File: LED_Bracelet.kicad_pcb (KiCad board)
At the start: 4 copper layers, 37.2 x 32.5 mm, 43 parts, among them J1 USB-C (Female), J2 LED Strip, J3 LED Filament, Q1 Si2301CDS, SW1 BOOT, U1 TP4056, U2 DW01A-G, U3 FS8205A, U4 TPS61170, U5 SN74AHCT1G125DBVR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

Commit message: Tweaks to the PCB
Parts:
- added H1: MountingHole_Pad, Custom:JLCPCB ToolingHole, F.Cu at (94.5, 38.7)
- added H2: MountingHole_Pad, Custom:JLCPCB ToolingHole, F.Cu at (63.5, 68.2)
- moved R14 1.59 mm to (98.5, 43.9), turned to 90 degrees
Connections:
- R14 pad 2: GND -> +BATT
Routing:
- net -BATT: track 21.2 -> 7.09 mm
- net +BATT: track 19.0 -> 21.3 mm, vias 4 -> 5
- net GND: track 31.2 -> 30.3 mm
- added copper zone on In2.Cu, net +5V
- added copper zone on In2.Cu, net -BATT
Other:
- board text added: "(analog)"
- board text added: "(digital)"
- board text added: "1A max"
- board text added: "1S LiPo USB-C ESP32-C3"
- board text added: "3v3"
- board text added: "5V"
- board text added: "BOOT"
- board text added: "ESP32-C3-WROOM-02"
- board text added: "LED Bracelet"
- board text added: "Power"
- board text added: "Standby Charging"
- board text added: "USB"
- board text added: "W"
- board text removed: "1S LiPo USB-C Multiple voltages"
- board text removed: "Rechargable Fan Controller"

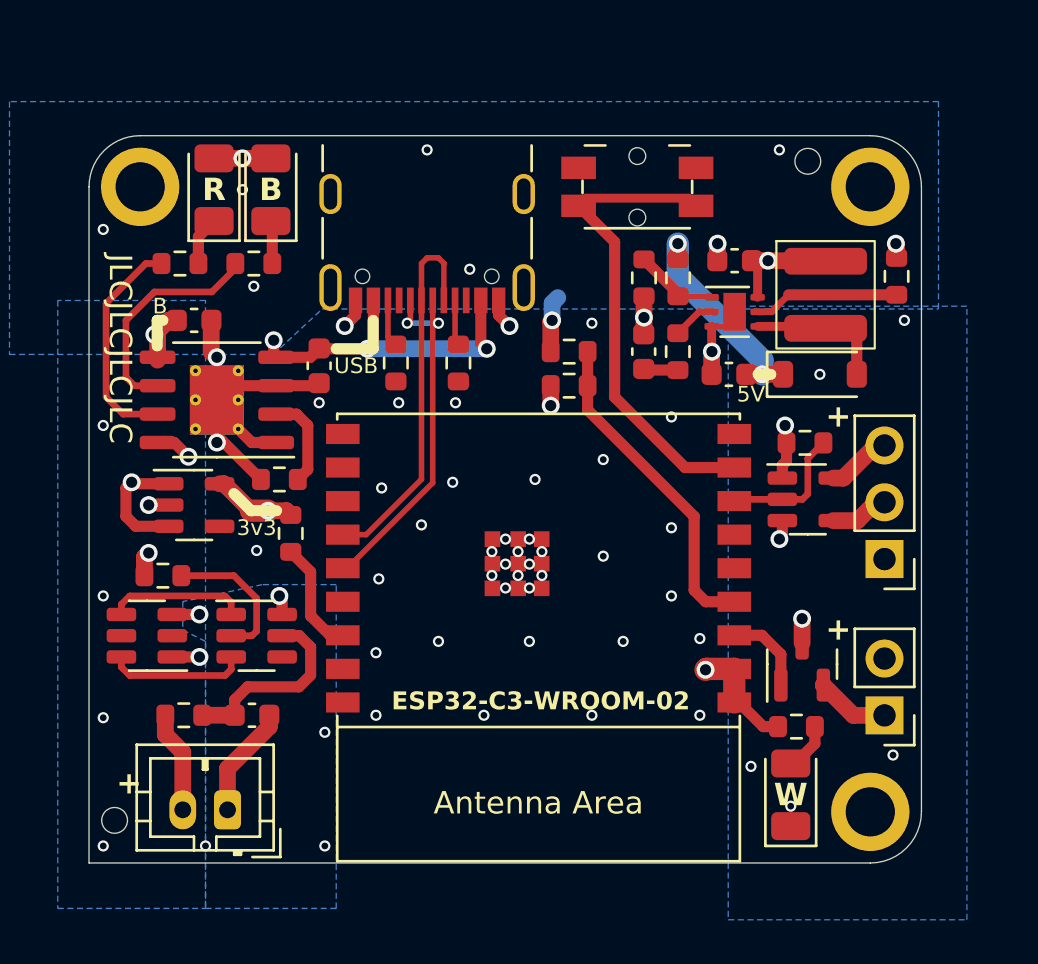
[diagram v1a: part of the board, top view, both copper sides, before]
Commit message: First software version + some PCB changes Separate BOOT and Mode buttons. LED Filament MOSFET (Q1) has pulldown resistor and is the correct channel. PlatformIO project + code. Frequently Asked Questions (FAQ).
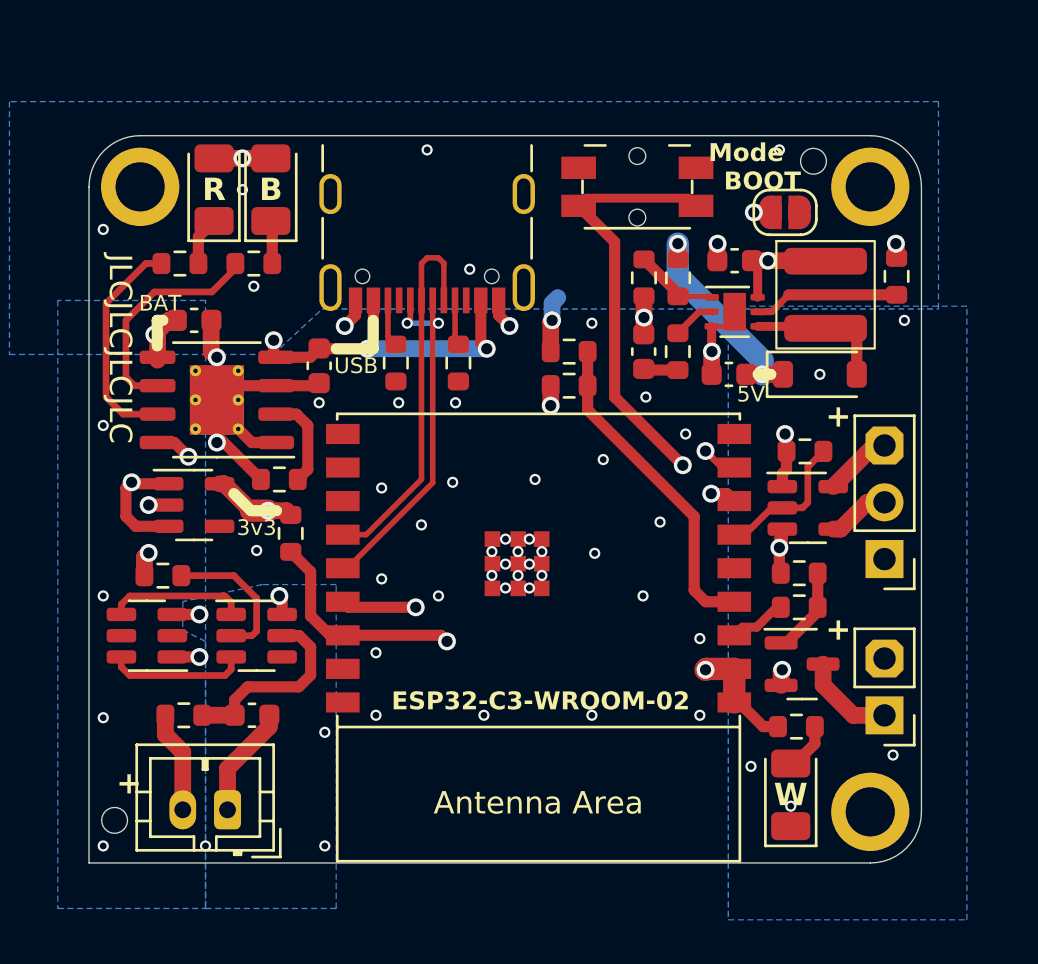
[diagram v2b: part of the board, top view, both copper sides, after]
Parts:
- added R17: 100R, Resistor_SMD:R_0603_1608Metric, F.Cu at (94.1, 58.7)
- added R18: 1k, Resistor_SMD:R_0603_1608Metric, F.Cu at (94.1, 57.1)
- added SW2: BOOT, Jumper:SolderJumper-2_P1.3mm_Open_RoundedPad1.0x1.5mm, F.Cu at (93.5, 41.0)
- Q1: value Si2301CDS -> AO3400A
- SW1: value BOOT -> Mode
- moved R11 0.38 mm to (94.4, 51.7)
- moved U5 0.38 mm to (94.5, 54.2)
- moved H1 0.25 mm to (94.7, 38.7)
- turned Q1 to 0 degrees
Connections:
- Q1 pad 1: LED Filament -> /Q1 Gate
- Q1 pad 2: Net-(J3-Pin_1) -> GND
- Q1 pad 3: GND -> Net-(J3-Pin_1)
- R12 pad 2: /Strapping 1 -> Strapping_1
- SW1 pad 2: /BOOT -> /Mode
- U6 pad 15: unconnected-(U6-GPIO3/ADC1_CH3-Pad15) -> /Mode
- U6 pad 16: /Strapping 1 -> Strapping_1
- U6 pad 6: unconnected-(U6-GPIO7-Pad6) -> LED Strip
- U6 pad 7: LED Strip -> Strapping_1
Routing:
- net /Mode: track 0.00 -> 40.8 mm, vias 0 -> 2
- net Strapping_1: track 0.00 -> 28.2 mm, vias 0 -> 2
- net /Strapping 1: track 5.03 -> 0.00 mm
- net /Q1 Gate: track 0.00 -> 3.93 mm
- net /BOOT: track 21.4 -> 19.3 mm, vias 0 -> 2
- net LED Filament: track 3.81 -> 2.60 mm
- net Net-(J3-Pin_1): track 3.30 -> 4.24 mm
- net GND: track 30.3 -> 31.1 mm, vias 68 -> 67
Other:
- board text added: "BAT"
- board text added: "Boot Jumper"
- board text added: "Mode"
- board text added: "Mode Button"
- board text removed: "BOOT Button"
